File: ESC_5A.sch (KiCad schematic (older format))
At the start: 23 parts, among them IC1 EEPROM, IC2 3.3V Reg, IC3 5V_Reg, IC4 ATSAMD21E17D-AUT, J1 USBc, J2 5V_PWR

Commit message: Leaving work for remote work
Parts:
- gave numbers to parts that had none: 1
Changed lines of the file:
@@
 	2150 5950 2150 7750
 $Comp
-L SamacSys_Parts:MPX1D0830L330 L?
+L SamacSys_Parts:MPX1D0830L330 L1
 U 1 1 60FE3DA9
 P 4950 5450
-F 0 "L?" H 5350 5675 50  0000 C CNN
+F 0 "L1" H 5350 5675 50  0000 C CNN
 F 1 "33uH" H 5350 5584 50  0000 C CNN
 F 2 "INDM8680X300N" H 5600 5500 50  0001 L CNN

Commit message: Remote work
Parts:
- C1, C8, C9: symbol SamacSys_Parts:GRM033R61C104KE84D -> ESC_5A-rescue:GRM033R61C104KE84D-SamacSys_Parts
- C2, C5, C6: symbol SamacSys_Parts:C1608X5R1C106M080AB -> ESC_5A-rescue:C1608X5R1C106M080AB-SamacSys_Parts
- C3: symbol SamacSys_Parts:GRT31CR61H106KE01L -> ESC_5A-rescue:GRT31CR61H106KE01L-SamacSys_Parts
- C4, C7: symbol SamacSys_Parts:GRM155C81C105KE11J -> ESC_5A-rescue:GRM155C81C105KE11J-SamacSys_Parts
- D2: symbol SamacSys_Parts:B340AE-13 -> ESC_5A-rescue:B340AE-13-SamacSys_Parts
- IC1: symbol SamacSys_Parts:AT25M02-SSHM-T -> ESC_5A-rescue:AT25M02-SSHM-T-SamacSys_Parts
- IC2: symbol SamacSys_Parts:AP2112M-3.3TRG1 -> ESC_5A-rescue:AP2112M-3.3TRG1-SamacSys_Parts
- IC3: symbol SamacSys_Parts:AP1501A-50K5G-13 -> ESC_5A-rescue:AP1501A-50K5G-13-SamacSys_Parts
- IC4: symbol SamacSys_Parts:ATSAMD21E17D-AUT -> ESC_5A-rescue:ATSAMD21E17D-AUT-SamacSys_Parts
- J1: symbol USB4105-GF-A:USB4105-GF-A -> ESC_5A-rescue:USB4105-GF-A-USB4105-GF-A
- L1: symbol SamacSys_Parts:MPX1D0830L330 -> ESC_5A-rescue:MPX1D0830L330-SamacSys_Parts
- S1: symbol SamacSys_Parts:LL3301NF065QG -> ESC_5A-rescue:LL3301NF065QG-SamacSys_Parts
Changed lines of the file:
@@
 $EndDescr
 $Comp
-L USB4105-GF-A:USB4105-GF-A J1
+L ESC_5A-rescue:USB4105-GF-A-USB4105-GF-A J1
 U 1 1 60CCC229
 P 2250 5200
@@
 $EndComp
 $Comp
-L SamacSys_Parts:ATSAMD21E17D-AUT IC4
+L ESC_5A-rescue:ATSAMD21E17D-AUT-SamacSys_Parts IC4
 U 1 1 60CD45A6
 P 8750 4150
@@
 USBc Connector
 $Comp
-L SamacSys_Parts:AP1501A-50K5G-13 IC3
+L ESC_5A-rescue:AP1501A-50K5G-13-SamacSys_Parts IC3
 U 1 1 60D0E744
 P 5050 4550
@@
 	9650 3300 9650 3350
 $Comp
-L SamacSys_Parts:AP2112M-3.3TRG1 IC2
+L ESC_5A-rescue:AP2112M-3.3TRG1-SamacSys_Parts IC2
 U 1 1 60D2104E
 P 4950 6850
@@
 	9750 3350 9750 3300
 $Comp
-L SamacSys_Parts:AT25M02-SSHM-T IC1
+L ESC_5A-rescue:AT25M02-SSHM-T-SamacSys_Parts IC1
 U 1 1 60E26D23
 P 4950 3550
@@
 EEPROM
 $Comp
-L SamacSys_Parts:GRM033R61C104KE84D C1
+L ESC_5A-rescue:GRM033R61C104KE84D-SamacSys_Parts C1
 U 1 1 60F10D35
 P 1650 7450
@@
 $EndComp
 $Comp
-L SamacSys_Parts:GRM033R61C104KE84D C9
+L ESC_5A-rescue:GRM033R61C104KE84D-SamacSys_Parts C9
 U 1 1 60F1C7F6
 P 8750 6050
@@
 $EndComp
 $Comp
-L SamacSys_Parts:GRM033R61C104KE84D C8
+L ESC_5A-rescue:GRM033R61C104KE84D-SamacSys_Parts C8
 U 1 1 60F23883
 P 8550 3750
@@
 $EndComp
 $Comp
-L SamacSys_Parts:C1608X5R1C106M080AB C2
+L ESC_5A-rescue:C1608X5R1C106M080AB-SamacSys_Parts C2
 U 1 1 60F2B101
 P 3900 6900
@@
 	3900 6900 4450 6900
 $Comp
-L SamacSys_Parts:C1608X5R1C106M080AB C6
+L ESC_5A-rescue:C1608X5R1C106M080AB-SamacSys_Parts C6
 U 1 1 60F417E2
 P 6500 6900
@@
 $EndComp
 $Comp
-L SamacSys_Parts:C1608X5R1C106M080AB C5
+L ESC_5A-rescue:C1608X5R1C106M080AB-SamacSys_Parts C5
 U 1 1 60F4C17B
 P 5800 5450
@@
 $EndComp
 $Comp
-L SamacSys_Parts:GRT31CR61H106KE01L C3
+L ESC_5A-rescue:GRT31CR61H106KE01L-SamacSys_Parts C3
 U 1 1 60F53AEE
 P 4450 4450
@@
 	4450 4450 5050 4450
 $Comp
-L SamacSys_Parts:GRM155C81C105KE11J C4
+L ESC_5A-rescue:GRM155C81C105KE11J-SamacSys_Parts C4
 U 1 1 60F5BE6E
 P 4450 6900
@@
 Connection ~ 4450 6900
 $Comp
-L SamacSys_Parts:GRM155C81C105KE11J C7
+L ESC_5A-rescue:GRM155C81C105KE11J-SamacSys_Parts C7
 U 1 1 60F6B9BB
 P 8000 3250
@@
 	5750 5450 5800 5450
 $Comp
-L SamacSys_Parts:B340AE-13 D2
+L ESC_5A-rescue:B340AE-13-SamacSys_Parts D2
 U 1 1 60FB57B1
 P 4950 5350
@@
 	700  4200 700  7750
 $Comp
-L SamacSys_Parts:LL3301NF065QG S1
+L ESC_5A-rescue:LL3301NF065QG-SamacSys_Parts S1
 U 1 1 610975F8
 P 1050 7450
@@
 	2150 5950 2150 7750
 $Comp
-L SamacSys_Parts:MPX1D0830L330 L1
+L ESC_5A-rescue:MPX1D0830L330-SamacSys_Parts L1
 U 1 1 60FE3DA9
 P 4950 5450

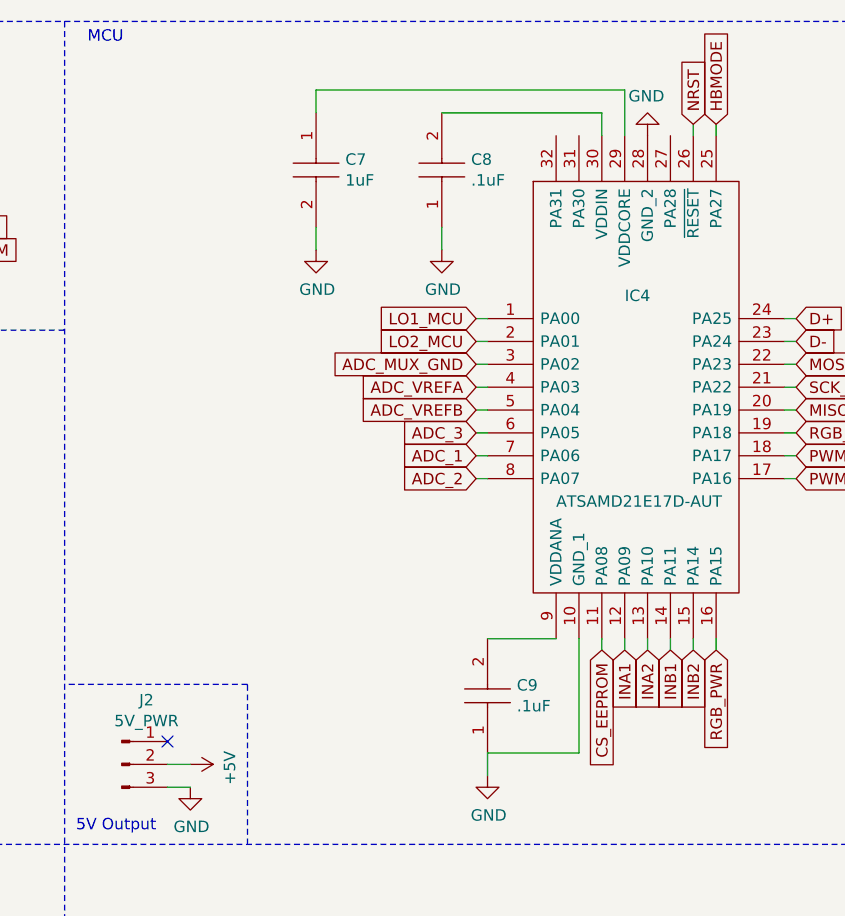
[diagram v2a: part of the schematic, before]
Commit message: Converted everything to XT30
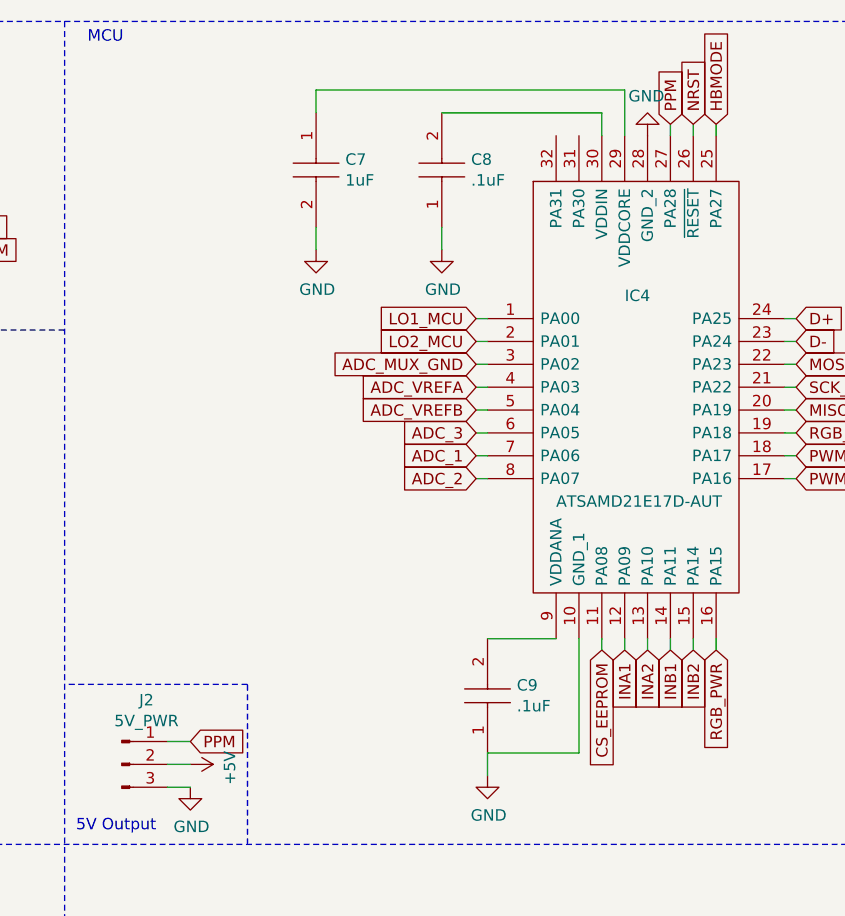
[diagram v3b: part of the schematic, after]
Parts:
- L1: footprint INDM8680X300N -> SamacSys_Parts:INDM8680X300N
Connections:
- net PPM: now reaches IC4.27 (PA28)
- net PPM: now also J2.1 (Pin_1)
- no-connect marks 7 -> 6
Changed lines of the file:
@@
 	0    1    1    0
 $EndComp
-NoConn ~ 7350 6000
 Wire Notes Line
 	7700 6450 7700 5750
@@
 F 0 "L1" H 5350 5675 50  0000 C CNN
 F 1 "33uH" H 5350 5584 50  0000 C CNN
-F 2 "INDM8680X300N" H 5600 5500 50  0001 L CNN
+F 2 "SamacSys_Parts:INDM8680X300N" H 5600 5500 50  0001 L CNN
 F 3 "https://componentsearchengine.com/Datasheets/1/MPX1D0830L330.pdf" H 5600 5400 50  0001 L CNN
 F 4 "Metal Composite Power Inductors MPX" H 5600 5300 50  0001 L CNN "Description"
@@
 $EndComp
 Connection ~ 4950 5450
+Wire Wire Line
+	7350 6000 7450 6000
+Text GLabel 7450 6000 2    50   Input ~ 0
+PPM
+Wire Wire Line
+	9550 3350 9550 3300
+Text GLabel 9550 3300 1    50   Input ~ 0
+PPM
 $EndSCHEMATC

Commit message: testing other options
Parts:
- L1: footprint SamacSys_Parts:INDM8680X300N -> SamacSys_Parts:XAL6060333MEC
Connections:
- net INA1: now also IC4.15 (PA14); no longer IC4.12 (PA09)
- net INA2: now also IC4.14 (PA11); no longer IC4.13 (PA10)
- net INB1: now also IC4.13 (PA10); no longer IC4.14 (PA11)
- net INB2: now also IC4.12 (PA09); no longer IC4.15 (PA14)
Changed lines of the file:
@@
 Text GLabel 10100 4750 2    50   Input ~ 0
 PWMB
+Text GLabel 9450 5600 3    50   Input ~ 0
+INB1
+Text GLabel 9350 5600 3    50   Input ~ 0
+INB2
+Text GLabel 9650 5600 3    50   Input ~ 0
+INA1
 Text GLabel 9550 5600 3    50   Input ~ 0
-INB1
-Text GLabel 9650 5600 3    50   Input ~ 0
-INB2
-Text GLabel 9350 5600 3    50   Input ~ 0
-INA1
-Text GLabel 9450 5600 3    50   Input ~ 0
 INA2
 Text GLabel 9750 3300 1    50   Input ~ 0
@@
 F 0 "L1" H 5350 5675 50  0000 C CNN
 F 1 "33uH" H 5350 5584 50  0000 C CNN
-F 2 "SamacSys_Parts:INDM8680X300N" H 5600 5500 50  0001 L CNN
+F 2 "SamacSys_Parts:XAL6060333MEC" H 5600 5500 50  0001 L CNN
 F 3 "https://componentsearchengine.com/Datasheets/1/MPX1D0830L330.pdf" H 5600 5400 50  0001 L CNN
 F 4 "Metal Composite Power Inductors MPX" H 5600 5300 50  0001 L CNN "Description"

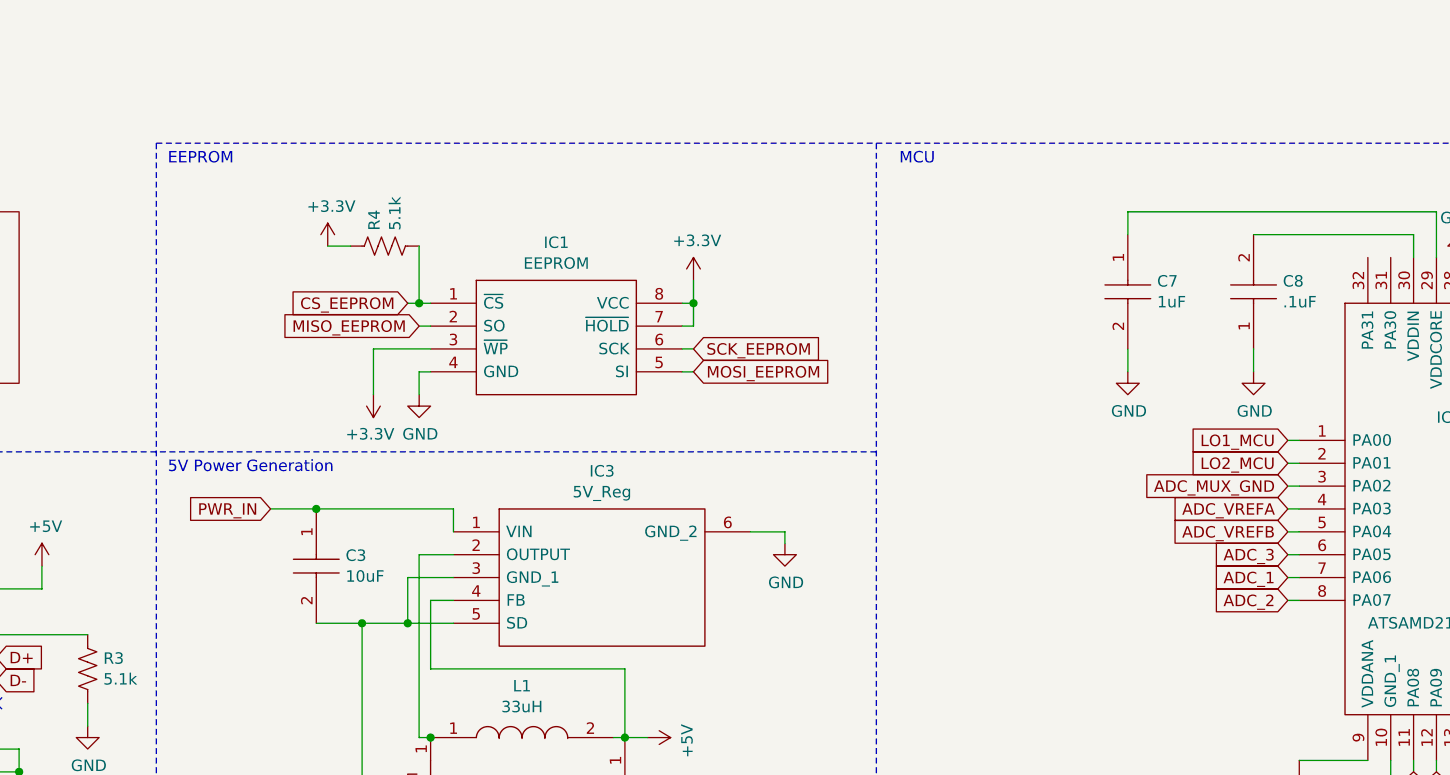
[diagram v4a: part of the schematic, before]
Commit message: Was able to shrink board another 6mm
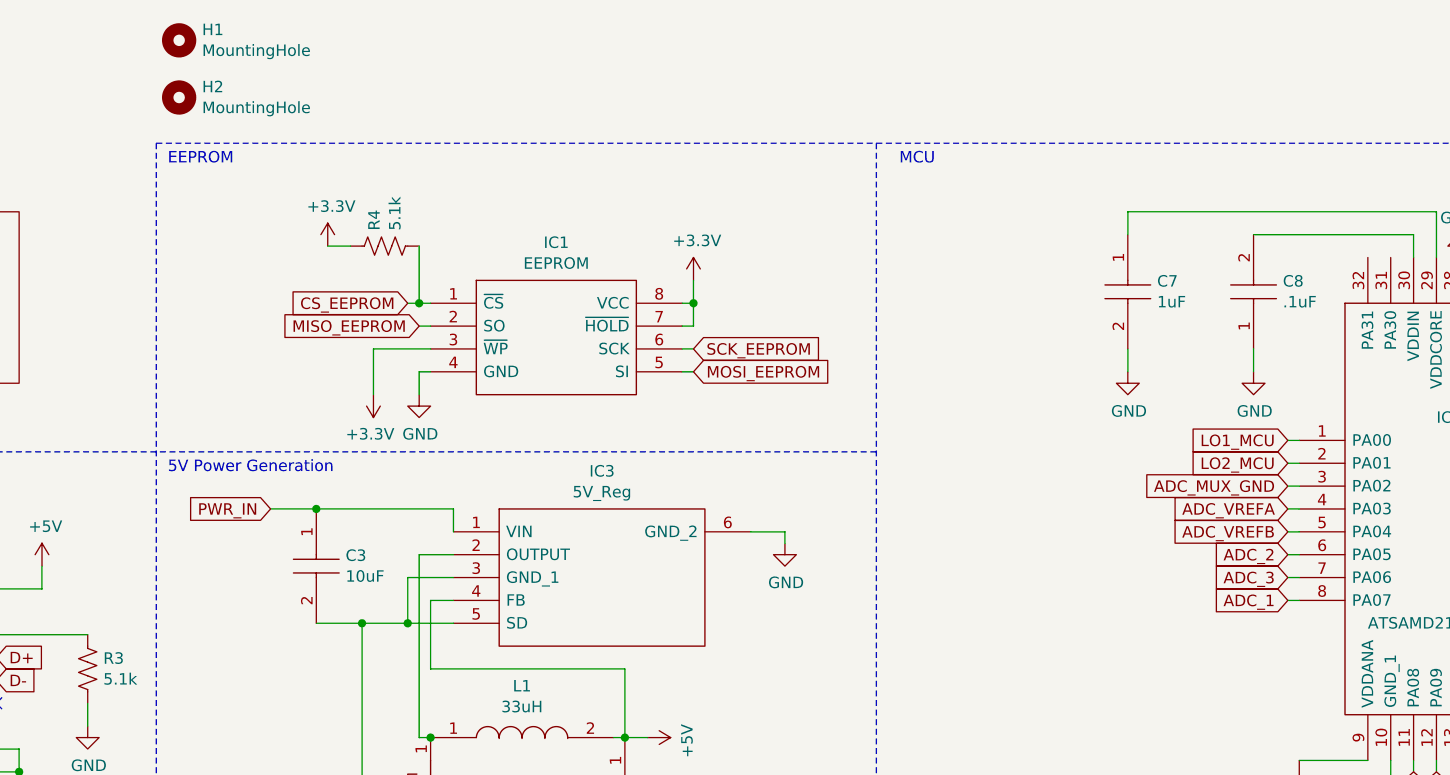
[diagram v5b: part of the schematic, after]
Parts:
- added H1, H2: MountingHole, MountingHole:MountingHole_2.2mm_M2, symbol Mechanical:MountingHole
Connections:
- net ADC_1: now also IC4.8 (PA07); no longer IC4.7 (PA06)
- net ADC_2: now also IC4.6 (PA05); no longer IC4.8 (PA07)
- net ADC_3: now also IC4.7 (PA06); no longer IC4.6 (PA05)
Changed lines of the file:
@@
 Text GLabel 8700 4550 0    50   Input ~ 0
 ADC_VREFB
-Text GLabel 8700 4750 0    50   Input ~ 0
+Text GLabel 8700 4850 0    50   Input ~ 0
 ADC_1
-Text GLabel 8700 4850 0    50   Input ~ 0
+Text GLabel 8700 4650 0    50   Input ~ 0
 ADC_2
 Text GLabel 8700 4350 0    50   Input ~ 0
 ADC_MUX_GND
-Text GLabel 8700 4650 0    50   Input ~ 0
+Text GLabel 8700 4750 0    50   Input ~ 0
 ADC_3
 Wire Wire Line
@@
 Text GLabel 9550 3300 1    50   Input ~ 0
 PPM
+$Comp
+L Mechanical:MountingHole H2
+U 1 1 60EFB1DF
+P 3850 2650
+F 0 "H2" H 3950 2696 50  0000 L CNN
+F 1 "MountingHole" H 3950 2605 50  0000 L CNN
+F 2 "MountingHole:MountingHole_2.2mm_M2" H 3850 2650 50  0001 C CNN
+F 3 "~" H 3850 2650 50  0001 C CNN
+	1    3850 2650
+	1    0    0    -1
+$EndComp
+$Comp
+L Mechanical:MountingHole H1
+U 1 1 60EFB7EF
+P 3850 2400
+F 0 "H1" H 3950 2446 50  0000 L CNN
+F 1 "MountingHole" H 3950 2355 50  0000 L CNN
+F 2 "MountingHole:MountingHole_2.2mm_M2" H 3850 2400 50  0001 C CNN
+F 3 "~" H 3850 2400 50  0001 C CNN
+	1    3850 2400
+	1    0    0    -1
+$EndComp
 $EndSCHEMATC

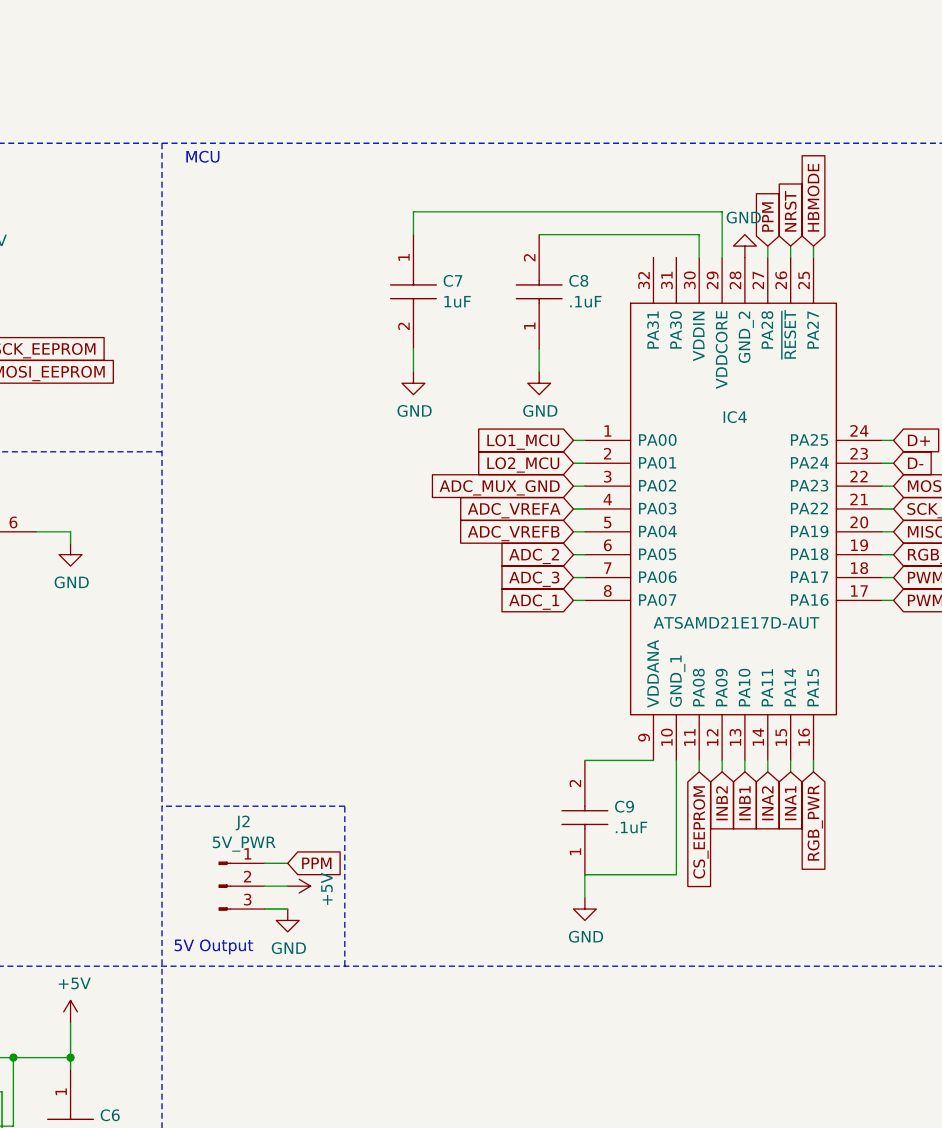
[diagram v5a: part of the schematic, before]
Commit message: Added second PPM input for indepedant motor control
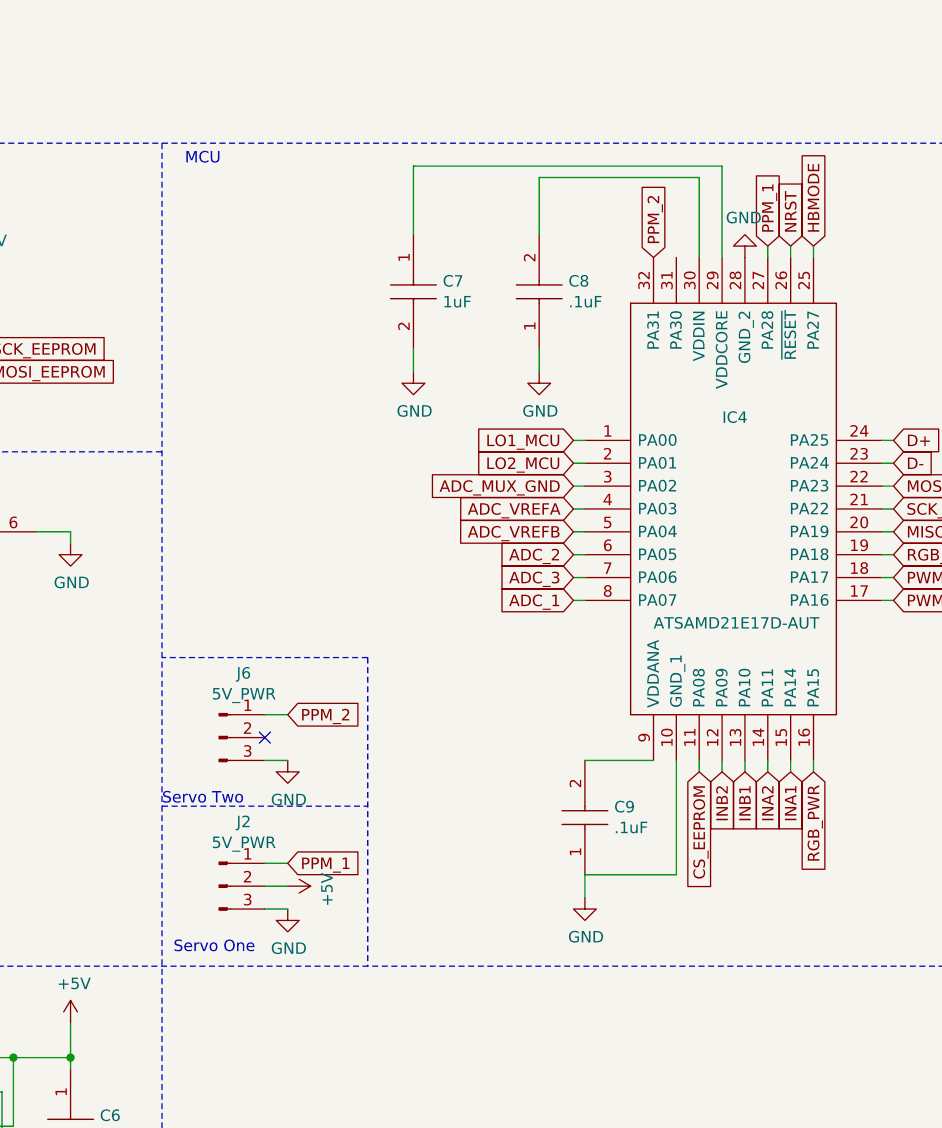
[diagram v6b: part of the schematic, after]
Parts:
- added J6: 5V_PWR, Connector_PinHeader_2.54mm:PinHeader_1x03_P2.54mm_Vertical, symbol Connector:Conn_01x03_Male
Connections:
- net GND: now also J6.3 (Pin_3)
- net PPM_2: now reaches IC4.32 (PA31)
- net PPM_2: now also J6.1 (Pin_1)
- net PPM renamed PPM_1
- no-connect marks 6 -> 7
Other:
- note added: "Servo One\n"
- note added: "Servo Two"
- note removed: "5V Output"
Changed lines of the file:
@@
 	1    0    0    -1
 $EndComp
-Wire Wire Line
-	9250 3350 9250 3250
-Wire Wire Line
-	9250 3250 8550 3250
 $Comp
 L power:GND #PWR024
@@
 Wire Wire Line
 	8550 3750 8550 3850
-Wire Wire Line
-	9350 3350 9350 3150
 $Comp
 L power:GND #PWR023
@@
 	0    1    1    0
 $EndComp
-Wire Notes Line
-	7700 6450 7700 5750
-Wire Notes Line
-	7700 5750 6900 5750
 Text Notes 3800 4300 0    50   ~ 0
 5V Power Generation
 Text Notes 6950 6400 0    50   ~ 0
-5V Output
+Servo One\n
 $Sheet
 S 1350 3150 1800 750
@@
 Wire Wire Line
 	9150 6050 8750 6050
-Wire Wire Line
-	9350 3150 8000 3150
-Wire Wire Line
-	8000 3150 8000 3250
 Wire Notes Line
 	11050 6450 11050 2850
@@
 	7350 6000 7450 6000
 Text GLabel 7450 6000 2    50   Input ~ 0
-PPM
+PPM_1
 Wire Wire Line
 	9550 3350 9550 3300
 Text GLabel 9550 3300 1    50   Input ~ 0
-PPM
+PPM_1
 $Comp
 L Mechanical:MountingHole H2
@@
 	1    0    0    -1
 $EndComp
+$Comp
+L Connector:Conn_01x03_Male J6
+U 1 1 60F759DB
+P 7150 5450
+F 0 "J6" H 7258 5731 50  0000 C CNN
+F 1 "5V_PWR" H 7258 5640 50  0000 C CNN
+F 2 "Connector_PinHeader_2.54mm:PinHeader_1x03_P2.54mm_Vertical" H 7150 5450 50  0001 C CNN
+F 3 "~" H 7150 5450 50  0001 C CNN
+	1    7150 5450
+	1    0    0    -1
+$EndComp
+Wire Wire Line
+	7350 5550 7450 5550
+$Comp
+L power:GND #PWR03
+U 1 1 60F79CEE
+P 7450 5550
+F 0 "#PWR03" H 7450 5300 50  0001 C CNN
+F 1 "GND" H 7455 5377 50  0000 C CNN
+F 2 "" H 7450 5550 50  0001 C CNN
+F 3 "" H 7450 5550 50  0001 C CNN
+	1    7450 5550
+	1    0    0    -1
+$EndComp
+Wire Wire Line
+	7350 5350 7450 5350
+Text GLabel 7450 5350 2    50   Input ~ 0
+PPM_2
+NoConn ~ 7350 5450
+Wire Notes Line
+	6900 5750 7800 5750
+Wire Notes Line
+	7800 5100 6900 5100
+Wire Notes Line
+	7800 5100 7800 6450
+Text Notes 6900 5750 0    50   ~ 0
+Servo Two
+Text GLabel 9050 3350 1    50   Input ~ 0
+PPM_2
+Wire Wire Line
+	9250 3000 8550 3000
+Wire Wire Line
+	8550 3000 8550 3250
+Wire Wire Line
+	9250 3000 9250 3350
+Wire Wire Line
+	9350 2950 8000 2950
+Wire Wire Line
+	9350 2950 9350 3350
+Wire Wire Line
+	8000 2950 8000 3250
 $EndSCHEMATC
